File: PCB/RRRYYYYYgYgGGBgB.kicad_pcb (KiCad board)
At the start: 2 copper layers, 24 x 24 mm, 36 parts, among them K1 CONN_6, SW1 SPST, SW2 SW_PUSH, SW3 SW_PUSH, U1 ATTINY85-M, U2 AAT1217-3.3, U3 74HC595, U4 74HC595

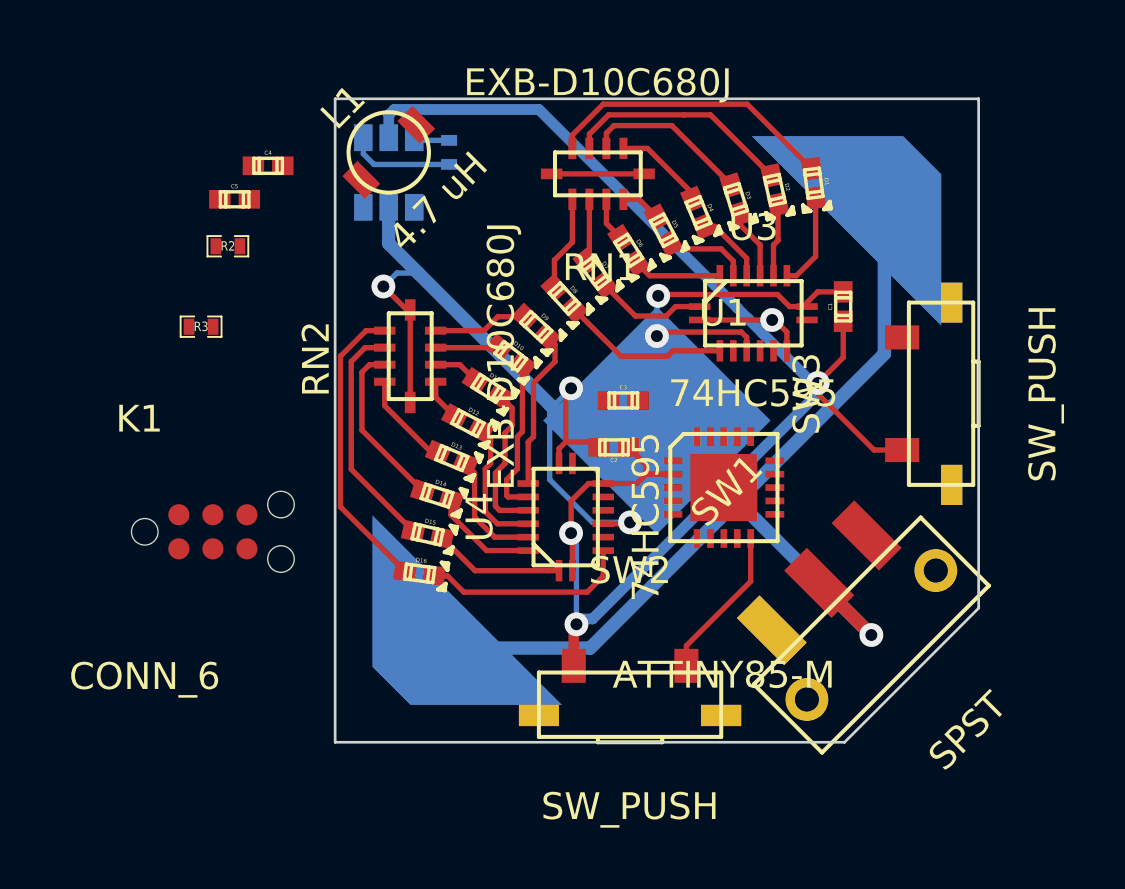
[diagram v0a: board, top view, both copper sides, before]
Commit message: moved a bunch of traces around and slightly reduced the rats nest.
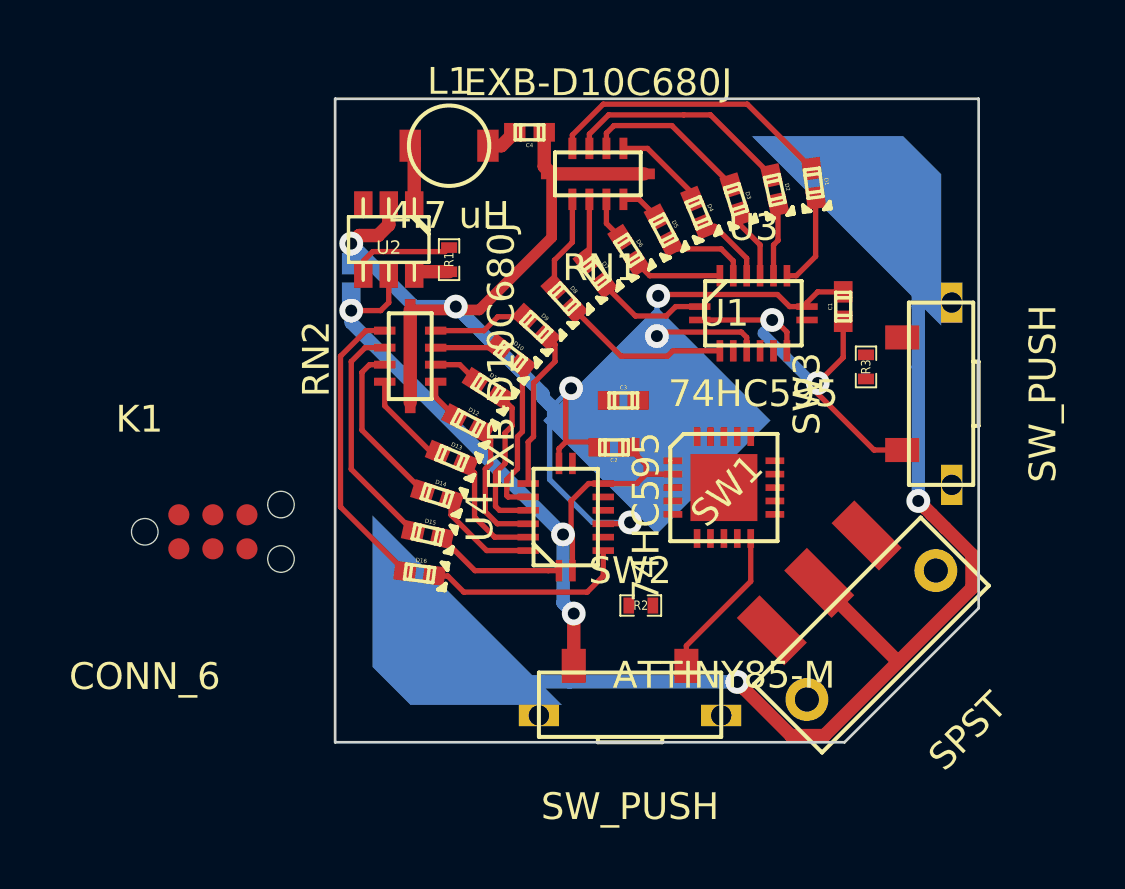
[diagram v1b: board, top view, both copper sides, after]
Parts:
- C5: moved to B.Cu
- R1, U2: moved to F.Cu
- moved R3 24.8 mm to (119.8, 34.0), turned to 90 degrees
- moved R2 20.4 mm to (111.4, 42.9)
- moved C4 9.83 mm to (107.2, 25.2), turned to 180 degrees
- moved C5 5.26 mm to (100.6, 30.7), turned to 270 degrees
- moved R1 4.00 mm to (104.2, 30.0), turned to 90 degrees
- moved U2 2.50 mm to (102.0, 29.2)
- moved L1 2.26 mm to (104.2, 25.8), turned to 0 degrees
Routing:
- net VCC: track 59.4 -> 43.3 mm, vias 4 -> 5
- net GND: track 56.2 -> 66.5 mm, vias 5 -> 6
- net N-000006: track 37.3 -> 44.1 mm, vias 1 -> 2
- net N-0000012: track 0.00 -> 2.26 mm
- net N-0000013: track 1.34 -> 2.55 mm
